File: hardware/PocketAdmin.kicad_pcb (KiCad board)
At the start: 2 copper layers, 15 x 31 mm, 21 parts, among them CON1 ST-LINK_V2, J1 USB_A_Plug, SW1 TL3342, U1 IP4220CZ6, U2 MCP1700-3302E_SOT23, U3 STM32F072C8Tx, U4 W25Q256FVFG, Y1 NX5032GA 8MHz

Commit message: initial commit
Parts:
- C11: value 100nF -> 20pF
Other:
- board text added: "github.com/krakrukra/PocketAdmin"
- board text added: "rev_1.1"
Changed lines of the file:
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@@
   (general
     (thickness 1.6)
-    (drawings 4)
+    (drawings 6)
     (tracks 192)
     (zones 0)
@@
       (effects (font (size 1 1) (thickness 0.15)) (justify mirror))
     )
-    (fp_text value 100nF (at 0 -1.43) (layer B.Fab)
+    (fp_text value 20pF (at 0 -1.43) (layer B.Fab)
       (effects (font (size 1 1) (thickness 0.15)) (justify mirror))
     )
@@
     )
   )
+  (gr_text rev_1.1 (at 131.6 77.7 90) (layer F.SilkS)
+    (effects (font (size 0.8 0.8) (thickness 0.15)))
+  )
+  (gr_text github.com/krakrukra/PocketAdmin (at 144 86.1 90) (layer F.SilkS)
+    (effects (font (size 0.8 0.8) (thickness 0.15)))
+  )
   (gr_line (start 130 101) (end 145 101) (layer Edge.Cuts) (width 0.15))

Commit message: initial commit
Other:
- board text removed: "github.com/krakrukra/PocketAdmin"
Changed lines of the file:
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@@
   (general
     (thickness 1.6)
-    (drawings 6)
+    (drawings 5)
     (tracks 192)
     (zones 0)
@@
     (effects (font (size 0.8 0.8) (thickness 0.15)))
   )
-  (gr_text github.com/krakrukra/PocketAdmin (at 144 86.1 90) (layer F.SilkS)
-    (effects (font (size 0.8 0.8) (thickness 0.15)))
-  )

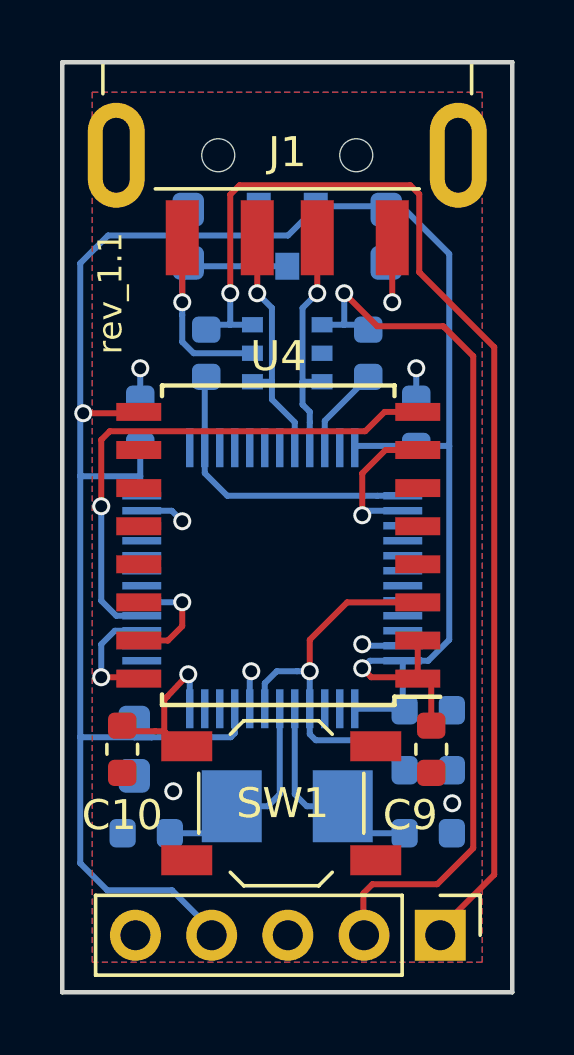
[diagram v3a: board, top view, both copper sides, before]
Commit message: small layout update
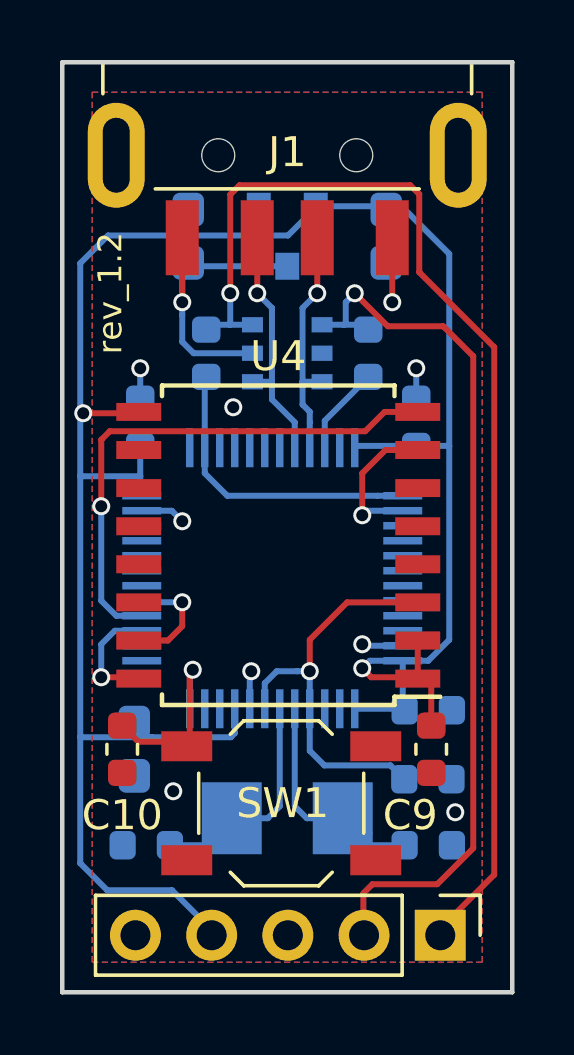
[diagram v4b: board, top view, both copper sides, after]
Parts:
- Y1: value NX5032GA 8MHz -> 8MHz
- moved Y1 0.40 mm to (137.5, 95.2)
- moved C4 0.40 mm to (142.2, 96.1)
- moved C5 0.40 mm to (132.8, 96.1)
- moved C11 0.30 mm to (142.2, 93.9)
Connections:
- U3 pad 2: Net-(U3-Pad2) -> GND
- U3 pad 28: Net-(U3-Pad28) -> GND
- U3 pad 30: Net-(U3-Pad30) -> GND
- U3 pad 39: Net-(U3-Pad39) -> GND
- U3 pad 41: Net-(U3-Pad41) -> GND
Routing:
- net Net-(C10-Pad2): track 5.82 -> 6.99 mm
- net GND: vias 8 -> 9
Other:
- board text added: "rev_1.2"
- board text removed: "rev_1.1"

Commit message: replaced tantalum capacitors with MLCC
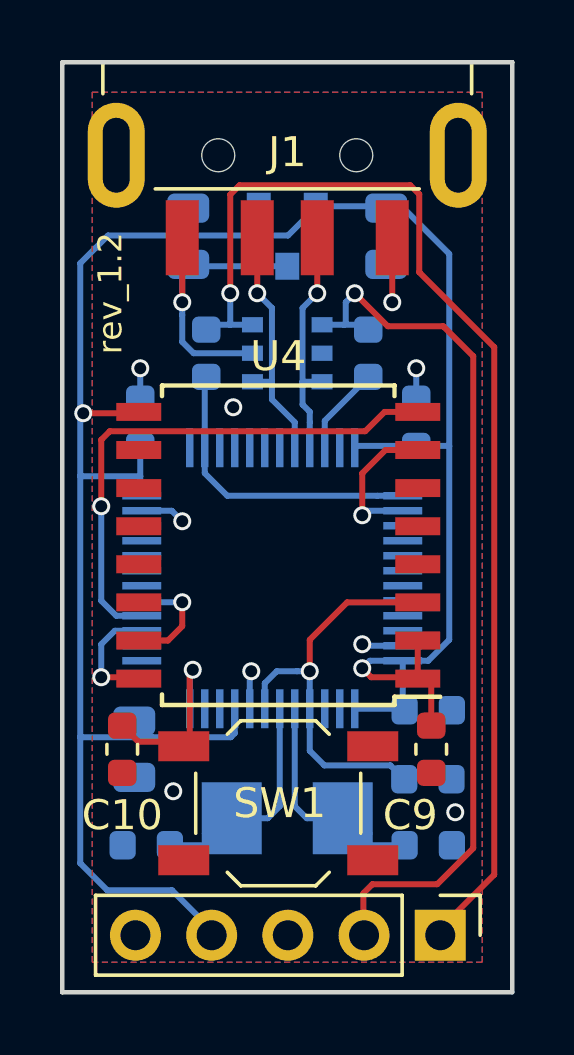
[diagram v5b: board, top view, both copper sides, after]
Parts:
- C1, C2, C8: footprint Capacitor_Tantalum_SMD:CP_EIA-2012-12_Kemet-R -> Capacitor_SMD:C_0805_2012Metric
- C10: value 20pF -> 100nF
- C11, C4, C5: value 20pF -> 18pF
- moved SW1 0.10 mm to (137.2, 94.7)

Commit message: added panelised verison of PCB
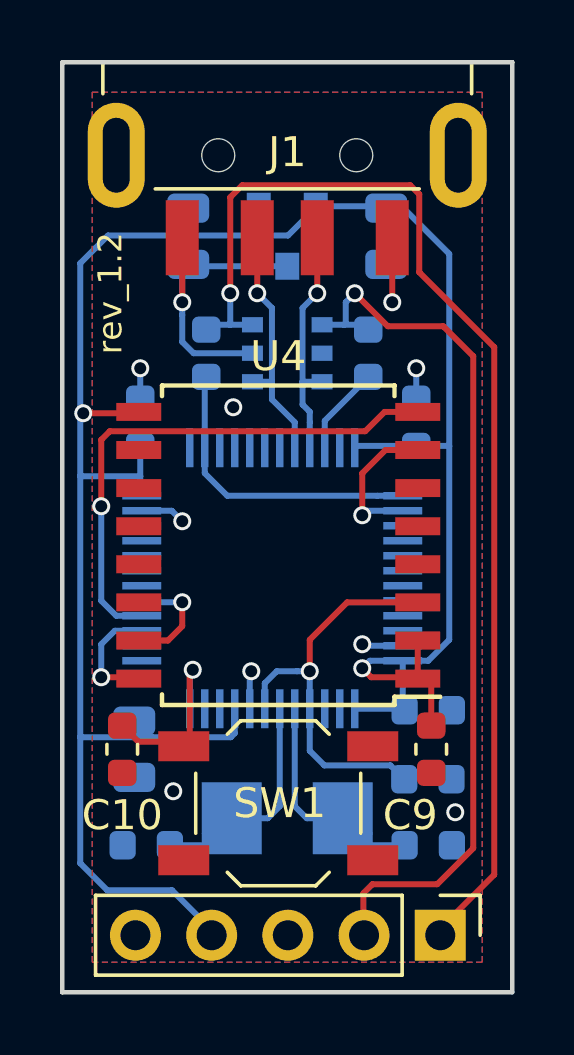
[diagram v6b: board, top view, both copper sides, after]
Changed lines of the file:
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@@
   (segment (start 144.4 97.08) (end 142.58 98.9) (width 0.2) (layer F.Cu) (net 4))
   (segment (start 144.4 79.5) (end 144.4 97.08) (width 0.2) (layer F.Cu) (net 4))
-  (segment (start 135.6 74.409998) (end 135.909998 74.1) (width 0.2) (layer F.Cu) (net 4))
-  (segment (start 135.6 77.7) (end 135.6 74.409998) (width 0.2) (layer F.Cu) (net 4))
-  (segment (start 135.909998 74.1) (end 141.6 74.1) (width 0.2) (layer F.Cu) (net 4))
+  (segment (start 135.6 77.7) (end 135.6 74.5) (width 0.2) (layer F.Cu) (net 4))
   (segment (start 141.6 74.1) (end 141.9 74.4) (width 0.2) (layer F.Cu) (net 4))
+  (segment (start 136 74.1) (end 141.6 74.1) (width 0.2) (layer F.Cu) (net 4))
+  (segment (start 135.6 74.5) (end 136 74.1) (width 0.2) (layer F.Cu) (net 4))
+  (segment (start 141.9 77) (end 144.4 79.5) (width 0.2) (layer F.Cu) (net 4))
   (segment (start 141.9 74.4) (end 141.9 77) (width 0.2) (layer F.Cu) (net 4))
-  (segment (start 141.9 77) (end 144.4 79.5) (width 0.2) (layer F.Cu) (net 4))
   (segment (start 140.1375 78.75) (end 140.2 78.8125) (width 0.2) (layer B.Cu) (net 5))
   (segment (start 139.4 78.75) (end 140.1375 78.75) (width 0.2) (layer B.Cu) (net 5))

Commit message: changed pad connection from solid to thermal
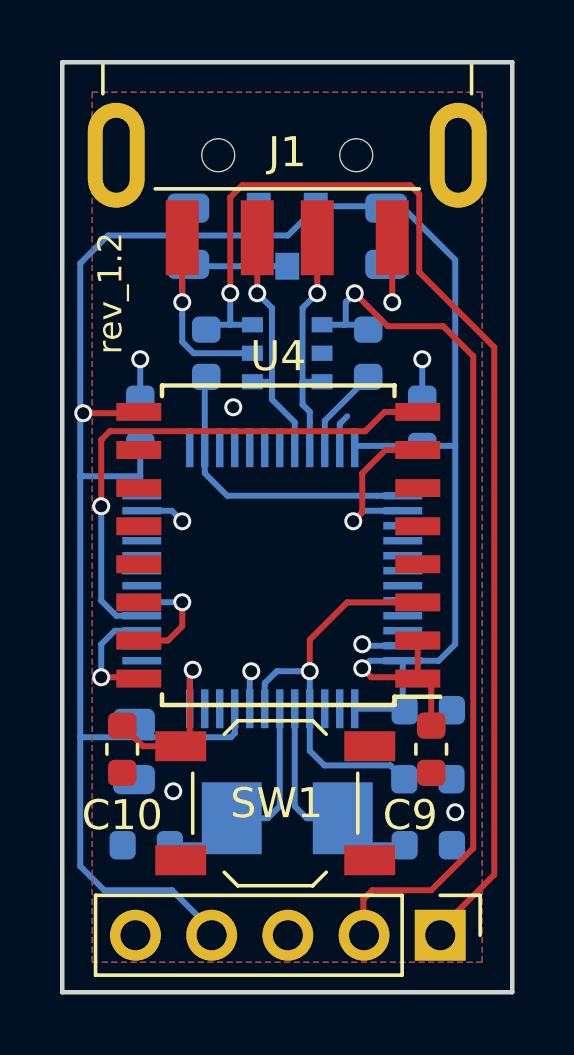
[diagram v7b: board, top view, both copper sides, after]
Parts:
- moved C3 0.20 mm to (142.0, 82.0)
- moved SW1 0.10 mm to (137.1, 94.7)
- moved C8 0.07 mm to (132.4, 93.0)
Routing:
- net GND: track 8.31 -> 9.76 mm
- net cs: track 4.98 -> 5.69 mm
- net 3.3V: track 79.9 -> 80.4 mm
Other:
- rule trace_min: 0.2 -> 0.19
